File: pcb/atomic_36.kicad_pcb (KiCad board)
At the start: 2 copper layers, 133.9 x 99 mm, 47 parts, among them J1 USB_C_12P

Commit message: Invert column GPIO order
When routing the board I boxed myself in :(.
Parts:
- removed MH1, MH2, MH3, MH4, MH5, MH6, MH7, MH8, MH9: , ceoloide:mounting_hole_npth
- added H1: , ceoloide:mounting_hole_plated, F.Cu at (156.7, 113.9)
- added H2: , ceoloide:mounting_hole_plated, F.Cu at (216.1, 107.4)
- added H3: , ceoloide:mounting_hole_plated, F.Cu at (230.4, 171.2)
- added H4: , ceoloide:mounting_hole_plated, F.Cu at (186.8, 148.9)
- added H5: , ceoloide:mounting_hole_plated, F.Cu at (159.8, 150.8)
- added H6: , ceoloide:mounting_hole_plated, F.Cu at (240.6, 98.7)
- added H7: , ceoloide:mounting_hole_plated, F.Cu at (263.2, 98.7)
- added H8: , ceoloide:mounting_hole_plated, F.Cu at (263.2, 155.8)
- added H9: , ceoloide:mounting_hole_plated, F.Cu at (240.6, 149.6)
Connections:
- S1 pad 1: GP15 -> GP11
- S10 pad 1: GP12 -> GP14
- S11 pad 1: GP12 -> GP14
- S12 pad 1: GP12 -> GP14
- S13 pad 1: GP11 -> GP15
- S14 pad 1: GP11 -> GP15
- S15 pad 1: GP11 -> GP15
- S17 pad 1: GP12 -> GP14
- S18 pad 1: GP11 -> GP15
- S2 pad 1: GP15 -> GP11
- S3 pad 1: GP15 -> GP11
- S4 pad 1: GP14 -> GP12
- S5 pad 1: GP14 -> GP12
- S6 pad 1: GP14 -> GP12
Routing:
- net GP29: track 0.00 -> 12.0 mm, vias 0 -> 5
- net GP28: track 0.00 -> 12.0 mm, vias 0 -> 5
- net GP27: track 0.00 -> 12.0 mm, vias 0 -> 5
- net GP15: track 24.8 -> 33.1 mm, vias 3 -> 4
- net GP12: track 33.1 -> 24.8 mm, vias 4 -> 3
- net GP14: track 24.8 -> 33.1 mm, vias 3 -> 4
- net GP11: track 33.1 -> 24.8 mm, vias 4 -> 3
- net GP26: track 0.00 -> 7.20 mm, vias 0 -> 3
- net pinky_top: track 19.1 -> 21.5 mm, vias 1 -> 2
- net mod_cluster: track 19.1 -> 21.5 mm, vias 1 -> 2
- net inner_home: track 19.1 -> 21.5 mm, vias 1 -> 2
- net inner_top: track 19.1 -> 21.5 mm, vias 1 -> 2
- net pinky_bottom: track 19.1 -> 21.5 mm, vias 1 -> 2
- net space_cluster: track 19.1 -> 21.5 mm, vias 1 -> 2
- net ring_bottom: track 19.1 -> 21.5 mm, vias 1 -> 2
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
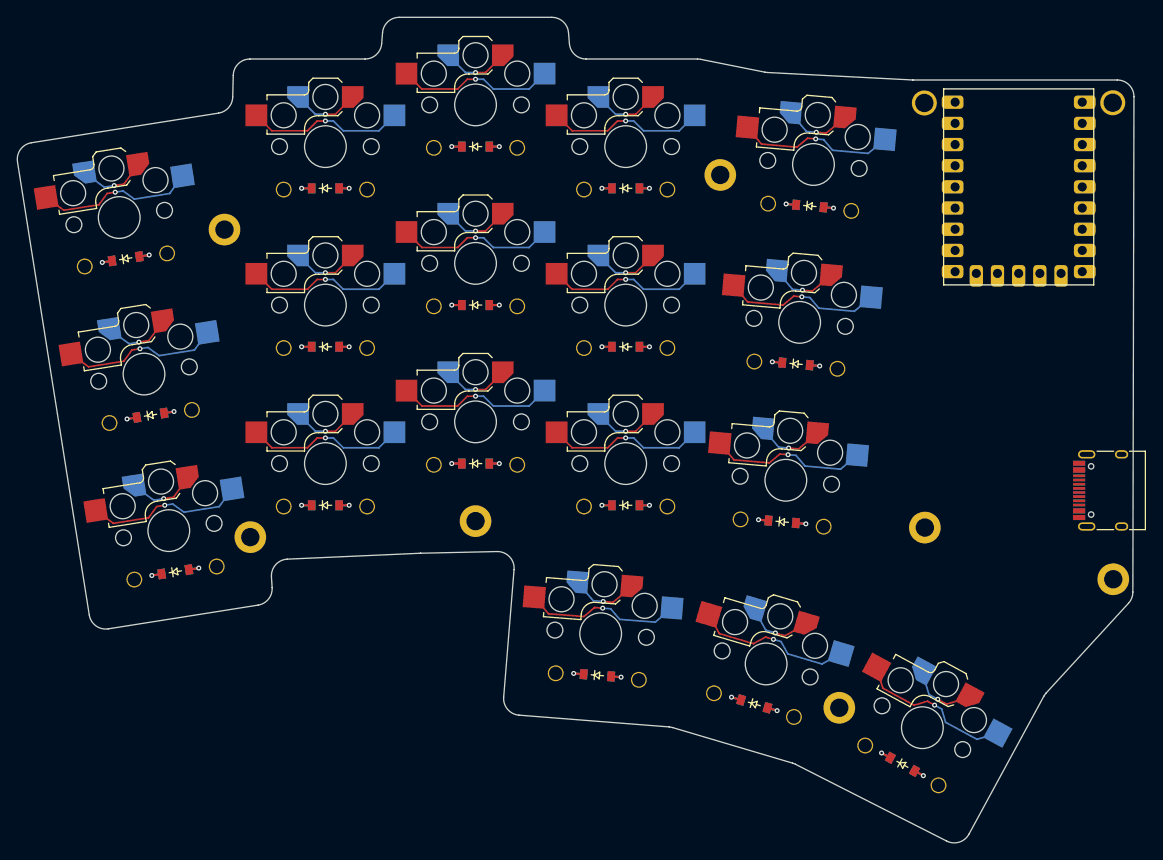
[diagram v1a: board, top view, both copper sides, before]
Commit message: Route the column matrix (back/right)
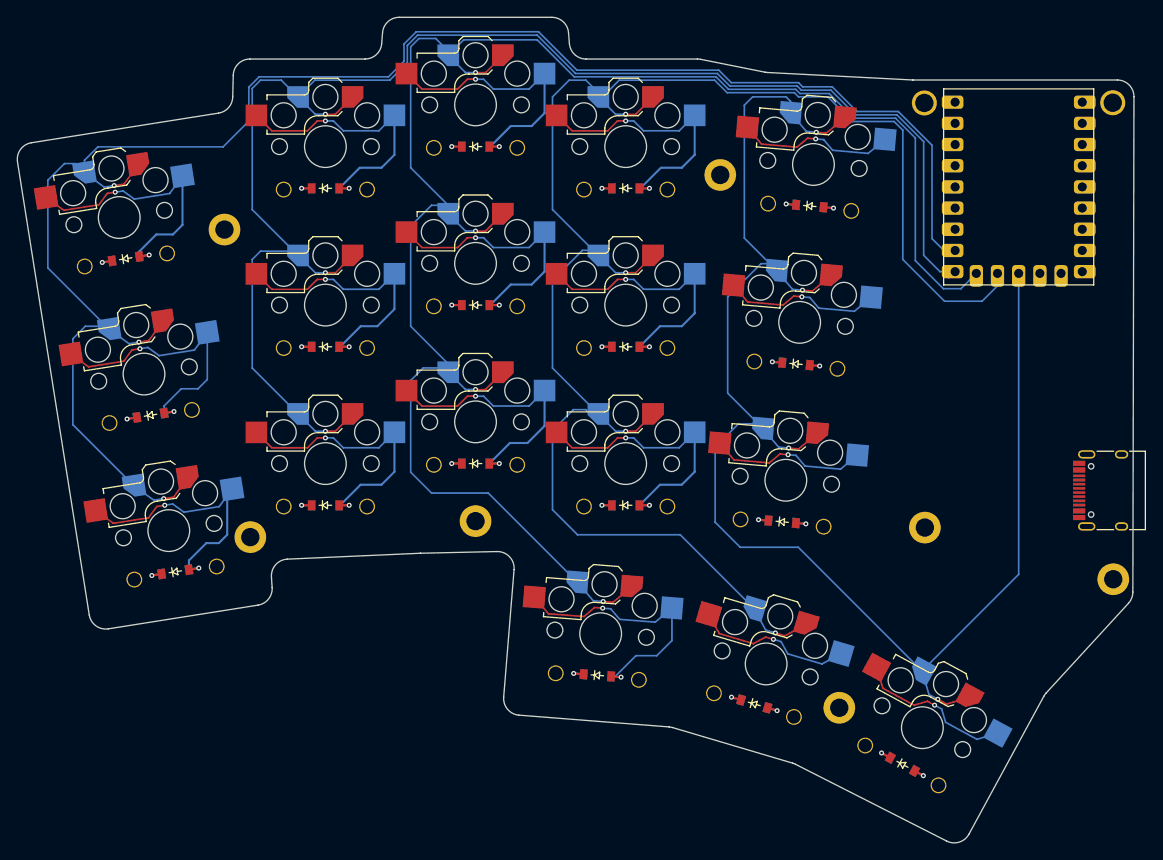
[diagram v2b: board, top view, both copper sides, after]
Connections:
- S1 pad 1: GP11 -> GP15
- S10 pad 1: GP14 -> GP12
- S11 pad 1: GP14 -> GP12
- S12 pad 1: GP14 -> GP12
- S13 pad 1: GP15 -> GP11
- S14 pad 1: GP15 -> GP11
- S15 pad 1: GP15 -> GP11
- S17 pad 1: GP14 -> GP12
- S18 pad 1: GP15 -> GP11
- S2 pad 1: GP11 -> GP15
- S3 pad 1: GP11 -> GP15
- S4 pad 1: GP12 -> GP14
- S5 pad 1: GP12 -> GP14
- S6 pad 1: GP12 -> GP14
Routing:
- net GP13: track 33.1 -> 213.9 mm
- net GP12: track 24.8 -> 203.7 mm, vias 3 -> 4
- net GP15: track 33.1 -> 210.5 mm, vias 4 -> 3
- net GP11: track 24.8 -> 188.2 mm, vias 3 -> 4
- net GP14: track 33.1 -> 184.6 mm, vias 4 -> 3
- net ring_top: track 21.5 -> 34.5 mm
- net middle_top: track 21.5 -> 34.5 mm
- net middle_home: track 21.5 -> 34.5 mm
- net index_top: track 21.5 -> 34.5 mm
- net index_home: track 21.5 -> 34.5 mm
- net ring_bottom: track 21.5 -> 34.5 mm
- net index_bottom: track 21.5 -> 34.5 mm
- net pinky_top: track 21.5 -> 34.5 mm
- net pinky_home: track 21.5 -> 34.5 mm
- net mod_cluster: track 21.5 -> 34.4 mm
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
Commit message: Complete column (back) routing
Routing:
- net inner_top: track 21.5 -> 34.6 mm
- net inner_bottom: track 21.5 -> 34.5 mm
- net inner_home: track 21.5 -> 34.4 mm
- net space_cluster: track 21.5 -> 34.1 mm
- net layer_cluster: track 21.5 -> 34.0 mm
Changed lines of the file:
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@@
+	)
+	(segment
+		(start 235.85632 107.14368)
+		(end 235.85632 103.094241)
+		(width 0.2)
+		(layer "B.Cu")
+		(net "inner_top")
 	)
 	(segment
@@
 	)
 	(segment
+		(start 228.493917 111.233538)
+		(end 230.727455 109)
+		(width 0.2)
+		(layer "B.Cu")
+		(net "inner_top")
+	)
+	(segment
+		(start 230.727455 109)
+		(end 234 109)
+		(width 0.2)
+		(layer "B.Cu")
+		(net "inner_top")
+	)
+	(segment
 		(start 229.583244 104.4065)
 		(end 228.511487 103.12923)
@@
 	)
 	(segment
+		(start 234 109)
+		(end 235.85632 107.14368)
+		(width 0.2)
+		(layer "B.Cu")
+		(net "inner_top")
+	)
+	(segment
 		(start 206.424057 127.964156)
 		(end 207.624057 127.964156)
@@
 	)
 	(segment
+		(start 225.181999 149.088936)
+		(end 225.411064 149.088936)
+		(width 0.25)
+		(layer "B.Cu")
+		(net "inner_bottom")
+	)
+	(segment
 		(start 230.53587 142.634998)
 		(end 226.271326 142.261899)
@@
 	)
 	(segment
+		(start 225.411064 149.088936)
+		(end 227.5 147)
+		(width 0.25)
+		(layer "B.Cu")
+		(net "inner_bottom")
+	)
+	(segment
+		(start 227.5 147)
+		(end 230.5 147)
+		(width 0.25)
+		(layer "B.Cu")
+		(net "inner_bottom")
+	)
+	(segment
 		(start 226.271326 142.261899)
 		(end 225.199569 140.984628)
@@
 	)
 	(segment
+		(start 230.5 147)
+		(end 232.544402 144.955598)
+		(width 0.25)
+		(layer "B.Cu")
+		(net "inner_bottom")
+	)
+	(segment
 		(start 226.377433 149.193523)
 		(end 225.181999 149.088936)
@@
 	)
 	(segment
+		(start 232.544402 144.955598)
+		(end 232.544402 140.94964)
+		(width 0.25)
+		(layer "B.Cu")
+		(net "inner_bottom")
+	)
+	(segment
 		(start 199.775455 160.305)
 		(end 201.043324 159.222137)
@@
 	)
 	(segment
+		(start 205.5 165)
+		(end 208.5 165)
+		(width 0.2)
+		(layer "B.Cu")
+		(net "mod_cluster")
+	)
+	(segment
+		(start 208.5 165)
+		(end 210.31777 163.18223)
+		(width 0.2)
+		(layer "B.Cu")
+		(net "mod_cluster")
+	)
+	(segment
 		(start 210.31777 163.18223)
 		(end 210.31777 159.274965)
@@
 	)
 	(segment
+		(start 203.026675 167.478201)
+		(end 205.5 165.004876)
+		(width 0.2)
+		(layer "B.Cu")
+		(net "mod_cluster")
+	)
+	(segment
 		(start 202.973522 159.374047)
 		(end 202.015319 159.298635)
@@
 	)
 	(segment
-		(start 203.026675 167.478201)
-		(end 203.521799 167.478201)
-		(width 0.2)
-		(layer "B.Cu")
-		(net "mod_cluster")
-	)
-	(segment
 		(start 208.324021 160.977786)
 		(end 204.056384 160.641916)
@@
 	)
 	(segment
-		(start 203.521799 167.478201)
-		(end 206 165)
-		(width 0.2)
-		(layer "B.Cu")
-		(net "mod_cluster")
-	)
-	(segment
-		(start 206 165)
-		(end 208.5 165)
-		(width 0.2)
-		(layer "B.Cu")
-		(net "mod_cluster")
-	)
-	(segment
-		(start 208.5 165)
-		(end 210.31777 163.18223)
-		(width 0.2)
-		(layer "B.Cu")
-		(net "mod_cluster")
-	)
-	(segment
 		(start 210.317769 159.274965)
 		(end 208.324021 160.977786)
@@
 	)
 	(segment
+		(start 205.5 165.004876)
+		(end 205.5 165)
+		(width 0.2)
+		(layer "B.Cu")
+		(net "mod_cluster")
+	)
+	(segment
 		(start 198.353057 102.068156)
 		(end 202.620057 102.068156)
@@
 	)
 	(segment
+		(start 248.5 175.184413)
+		(end 249.403567 174.280846)
+		(width 0.25)
+		(layer "B.Cu")
+		(net "space_cluster")
+	)
+	(segment
 		(start 242.653962 171.384188)
 		(end 241.809273 170.925559)
@@
 	)
 	(segment
+		(start 239.406264 178.809319)
+		(end 239.690681 178.809319)
+		(width 0.25)
+		(layer "B.Cu")
+		(net "space_cluster")
+	)
+	(segment
+		(start 247 178)
+		(end 248.5 176.5)
+		(width 0.25)
+		(layer "B.Cu")
+		(net "space_cluster")
+	)
+	(segment
+		(start 248.5 176.5)
+		(end 248.5 175.184413)
+		(width 0.25)
+		(layer "B.Cu")
+		(net "space_cluster")
+	)
+	(segment
 		(start 243.127517 172.982883)
 		(end 242.653962 171.384188)
@@
 	)
 	(segment
+		(start 240.5 178)
+		(end 247 178)
+		(width 0.25)
+		(layer "B.Cu")
+		(net "space_cluster")
+	)
+	(segment
+		(start 239.690681 178.809319)
+		(end 240.5 178)
+		(width 0.25)
+		(layer "B.Cu")
+		(net "space_cluster")
+	)
+	(segment
 		(start 240.460845 179.38191)
 		(end 239.406264 178.809319)
@@
 	)
 	(segment
+		(start 234.200361 125.799639)
+		(end 234.200361 122.021941)
+		(width 0.2)
+		(layer "B.Cu")
+		(net "inner_home")
+	)
+	(segment
+		(start 228.999195 128)
+		(end 232 128)
+		(width 0.2)
+		(layer "B.Cu")
+		(net "inner_home")
+	)
+	(segment
+		(start 226.837958 130.161237)
+		(end 228.999195 128)
+		(width 0.2)
+		(layer "B.Cu")
+		(net "inner_home")
+	)
+	(segment
 		(start 226.855528 122.056929)
 		(end 225.89802 121.973158)
@@
 	)
 	(segment
+		(start 232 128)
+		(end 234.200361 125.799639)
+		(width 0.2)
+		(layer "B.Cu")
+		(net "inner_home")
+	)
+	(segment
 		(start 234.200361 122.02194)
 		(end 232.191829 123.707299)
@@
 	)
 	(segment
+		(start 230 165.354463)
+		(end 230.613721 164.740742)
+		(width 0.2)
+		(layer "B.Cu")
+		(net "layer_cluster")
+	)
+	(segment
 		(start 228.309505 165.991829)
 		(end 224.204956 164.776007)
@@
 	)
 	(segment
+		(start 230 167)
+		(end 230 165.354463)
+		(width 0.2)
+		(layer "B.Cu")
+		(net "layer_cluster")
+	)
+	(segment
+		(start 223.525218 169.5)
+		(end 227.5 169.5)
+		(width 0.2)
+		(layer "B.Cu")
+		(net "layer_cluster")
+	)
+	(segment
 		(start 224.204956 164.776007)
 		(end 223.409362 163.310704)
 		(width 0.2)
 		(layer "B.Cu")
+		(net "layer_cluster")
+	)
+	(segment
+		(start 221.776406 171.248812)
+		(end 223.525218 169.5)
+		(width 0.2)
+		(layer "B.Cu")
+		(net "layer_cluster")
+	)
+	(segment
+		(start 227.5 169.5)
+		(end 230 167)
+		(width 0.2)
+		(layer "B.Cu")

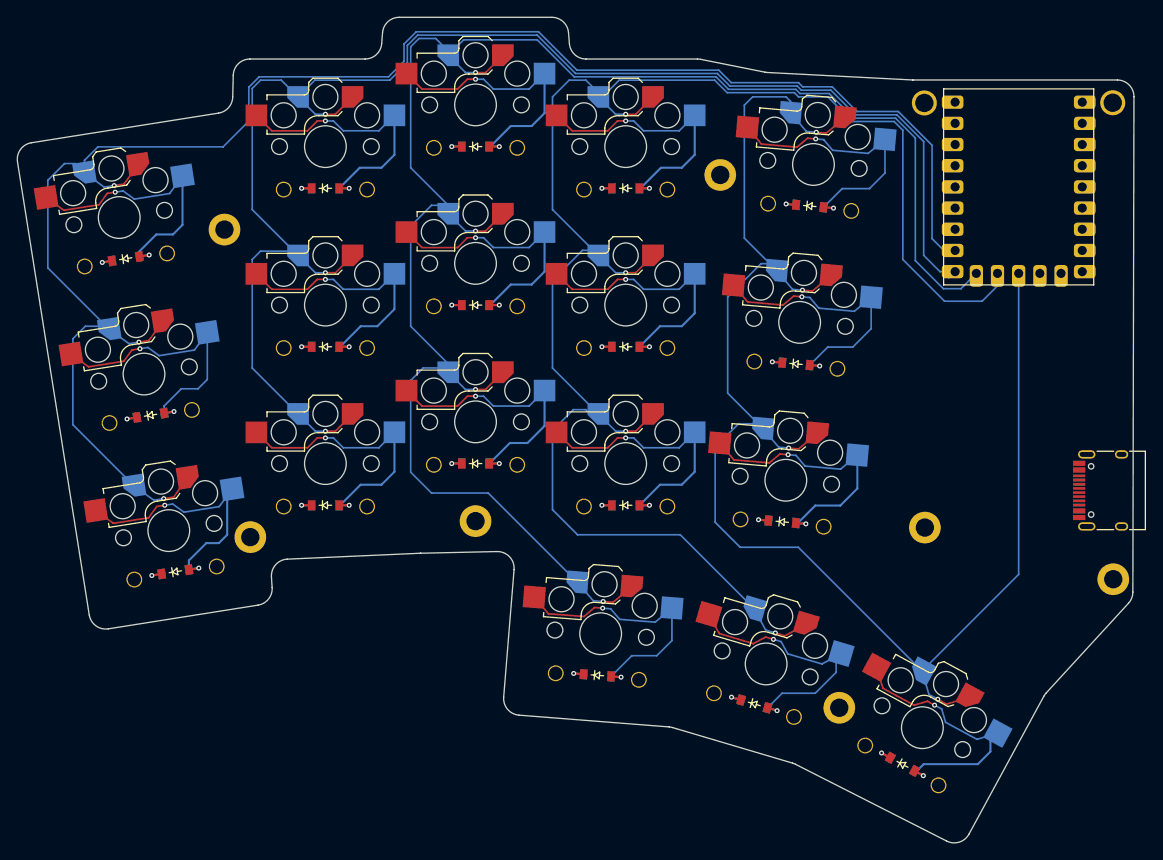
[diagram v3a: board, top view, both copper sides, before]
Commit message: Route rows (front)
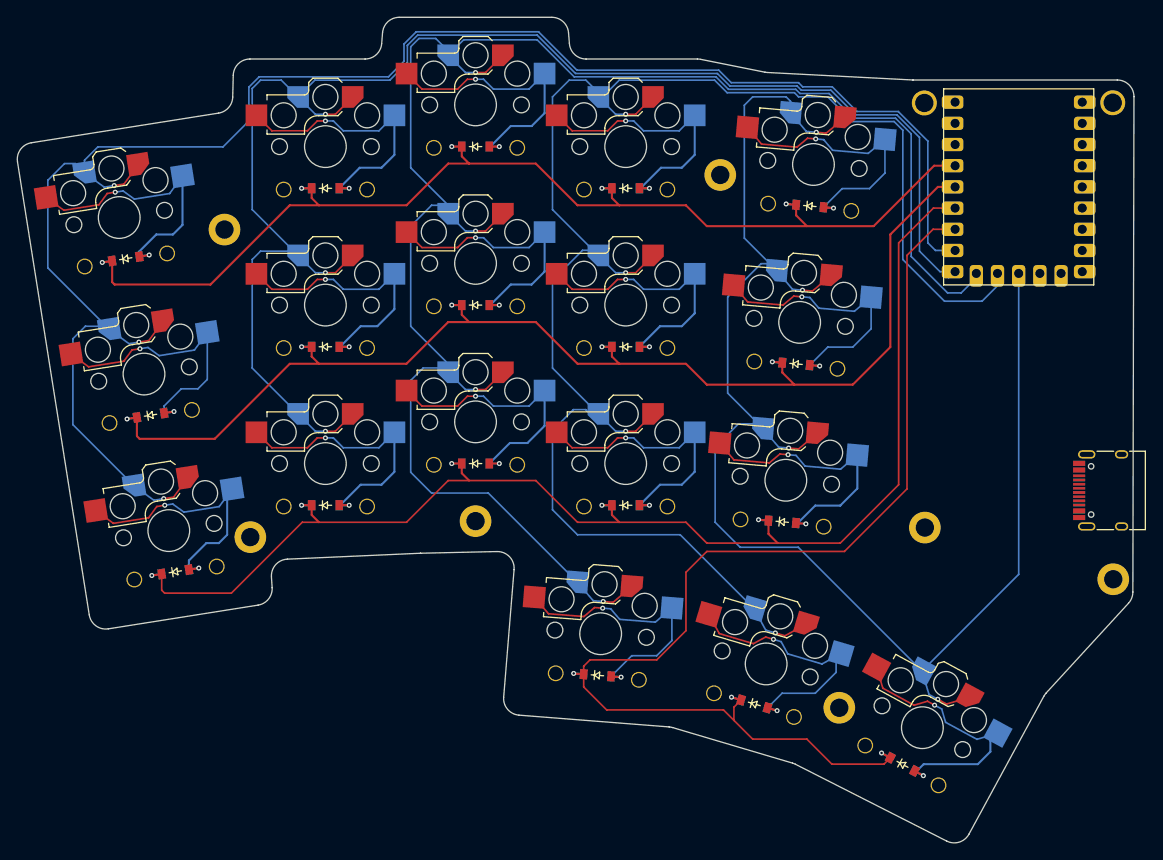
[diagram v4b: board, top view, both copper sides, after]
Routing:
- net GP27: track 12.0 -> 161.9 mm
- net GP28: track 12.0 -> 149.5 mm
- net GP26: track 7.20 -> 140.1 mm
- net GP29: track 12.0 -> 138.1 mm
- net GP13: track 213.9 -> 214.6 mm
- net GP15: track 210.5 -> 211.1 mm

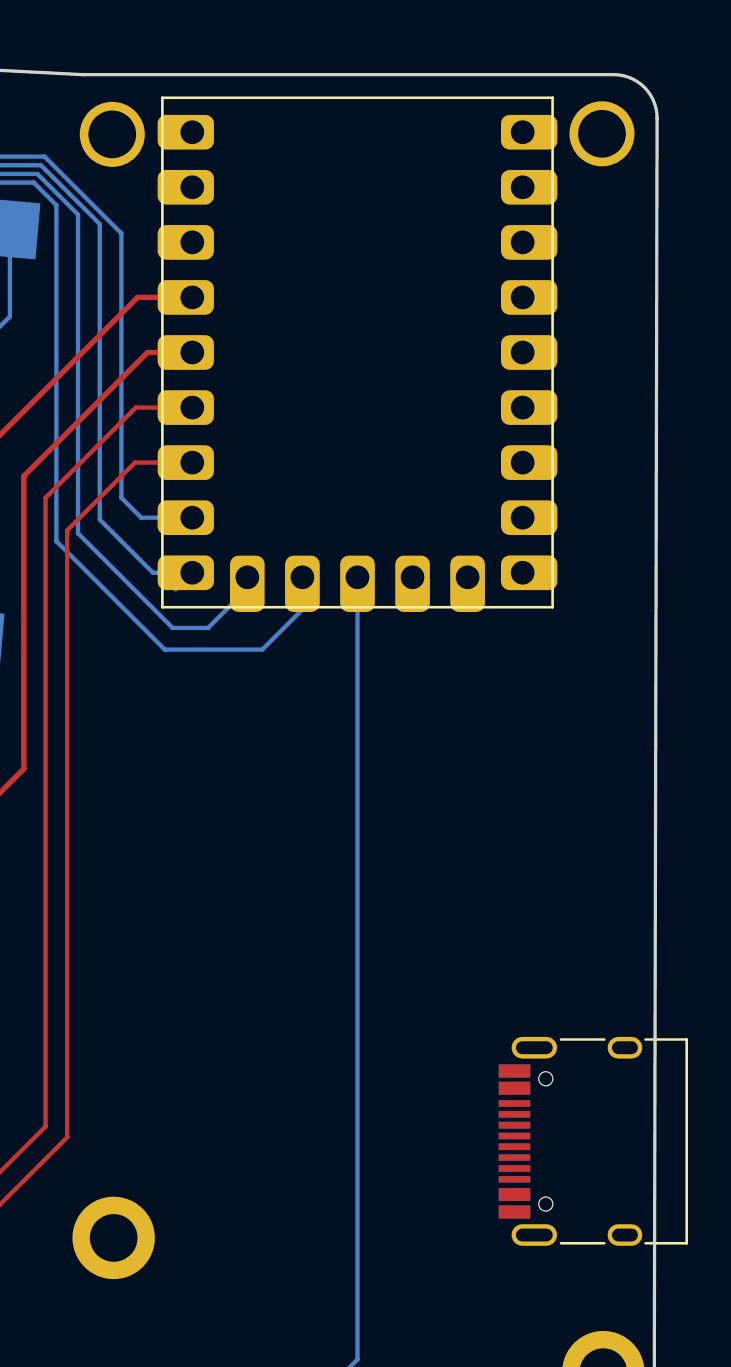
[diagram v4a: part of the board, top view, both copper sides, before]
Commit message: Route left (central) USB C
GP8 and GP9 are used as TX and RX. The pins are from
left to right:

- GND
- P5V
- BLANK
- GP8 (TX)
- GP9 (RX)
- BLANK
- BLANK
- GP9 (RX)
- GP8 (TX)
- BLANK
- P5V
- GND

GP8/9 belong to UART1
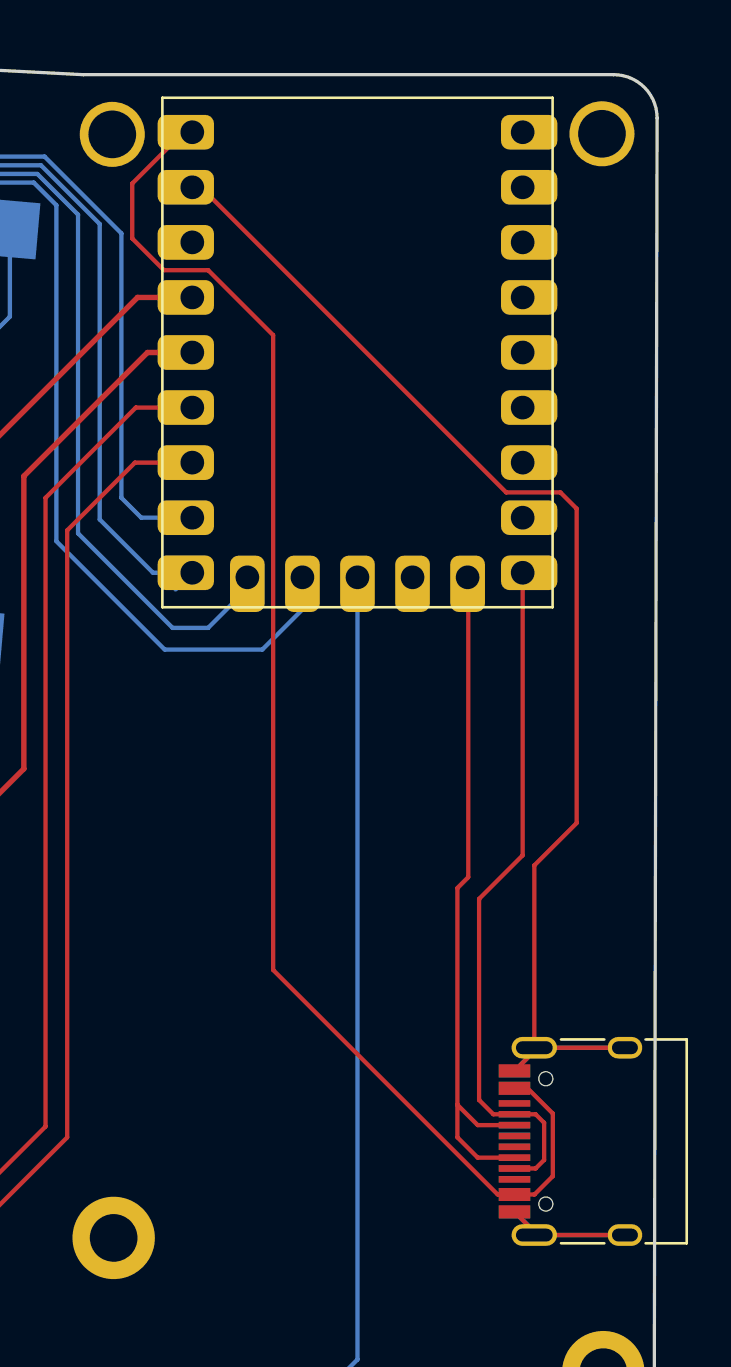
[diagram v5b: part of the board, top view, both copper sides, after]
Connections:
- J1 pad F11: VBUS -> P5V
- J1 pad F2: VBUS -> P5V
- J1 pad F4: (no net) -> GP8
- J1 pad F5: DM -> GP9
- J1 pad F6: DM -> (no net)
- J1 pad F7: DP -> (no net)
- J1 pad F8: DP -> GP9
- J1 pad F9: (no net) -> GP8
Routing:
- net GND: track 0.00 -> 71.8 mm
- net P5V: track 0.00 -> 66.6 mm
- net GP9: track 0.00 -> 32.1 mm
- net GP8: track 0.00 -> 31.8 mm
